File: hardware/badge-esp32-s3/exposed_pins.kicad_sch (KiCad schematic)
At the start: 0 parts

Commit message: JST PH and JST SH headers completed
Both subsheets are in exposed pins subsheet. I also had to make the symbols and footprints associated with each other.
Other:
- added sheet JST PH (JST-PH.kicad_sch)
- added sheet JST-SH (JST-SH.kicad_sch)
- note added: "Grove Link"
- note added: "Refrence Pics for both Grove, Stemma, Stemma QT"
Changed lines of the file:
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@@
 	(generator_version "9.0")
 	(paper "A4")
+	(text "Refrence Pics for both Grove, Stemma, Stemma QT\n "
+		(exclude_from_sim no)
+		(at 71.374 32.766 0)
+		(effects
+			(font
+				(size 1.27 1.27)
+			)
+			(href "https://www.cable-tester.com/category/pin-out/")
+		)
+	)
+	(text "Grove Link\n\n"
+		(exclude_from_sim no)
+		(at 57.912 27.94 0)
+		(effects
+			(font
+				(size 1.27 1.27)
+			)
+			(href "https://wiki.seeedstudio.com/Grove_System/")
+		)
+	)
+	(sheet
+		(at 80.01 40.64)
+		(size 20.32 10.16)
+		(exclude_from_sim no)
+		(in_bom yes)
+		(on_board yes)
+		(dnp no)
+		(fields_autoplaced yes)
+		(stroke
+			(width 0.1524)
+			(type solid)
+		)
+		(fill
+			(color 0 0 0 0.0000)
+		)
+		(property "Sheetname" "JST-SH"
+			(at 80.01 39.9284 0)
+			(effects
+				(font
+					(size 1.27 1.27)
+				)
+				(justify left bottom)
+			)
+		)
+		(property "Sheetfile" "JST-SH.kicad_sch"
+			(at 80.01 51.3846 0)
+			(effects
+				(font
+					(size 1.27 1.27)
+				)
+				(justify left top)
+			)
+		)
+		(instances
+			(project "badge-esp32-s3"
+				(path "/e2af9a6c-dbe9-4de2-9ba6-ea213a7300ec/069334c8-a377-4249-b519-18db4f2b1959"
+					(page "16")
+				)
+			)
+		)
+	)
+	(sheet
+		(at 44.45 40.64)
+		(size 21.59 10.16)
+		(exclude_from_sim no)
+		(in_bom yes)
+		(on_board yes)
+		(dnp no)
+		(fields_autoplaced yes)
+		(stroke
+			(width 0.1524)
+			(type solid)
+		)
+		(fill
+			(color 0 0 0 0.0000)
+		)
+		(property "Sheetname" "JST PH"
+			(at 44.45 39.9284 0)
+			(effects
+				(font
+					(size 1.27 1.27)
+				)
+				(justify left bottom)
+			)
+		)
+		(property "Sheetfile" "JST-PH.kicad_sch"
+			(at 44.45 51.3846 0)
+			(effects
+				(font
+					(size 1.27 1.27)
+				)
+				(justify left top)
+			)
+		)
+		(instances
+			(project "badge-esp32-s3"
+				(path "/e2af9a6c-dbe9-4de2-9ba6-ea213a7300ec/069334c8-a377-4249-b519-18db4f2b1959"
+					(page "15")
+				)
+			)
+		)
+	)
 )

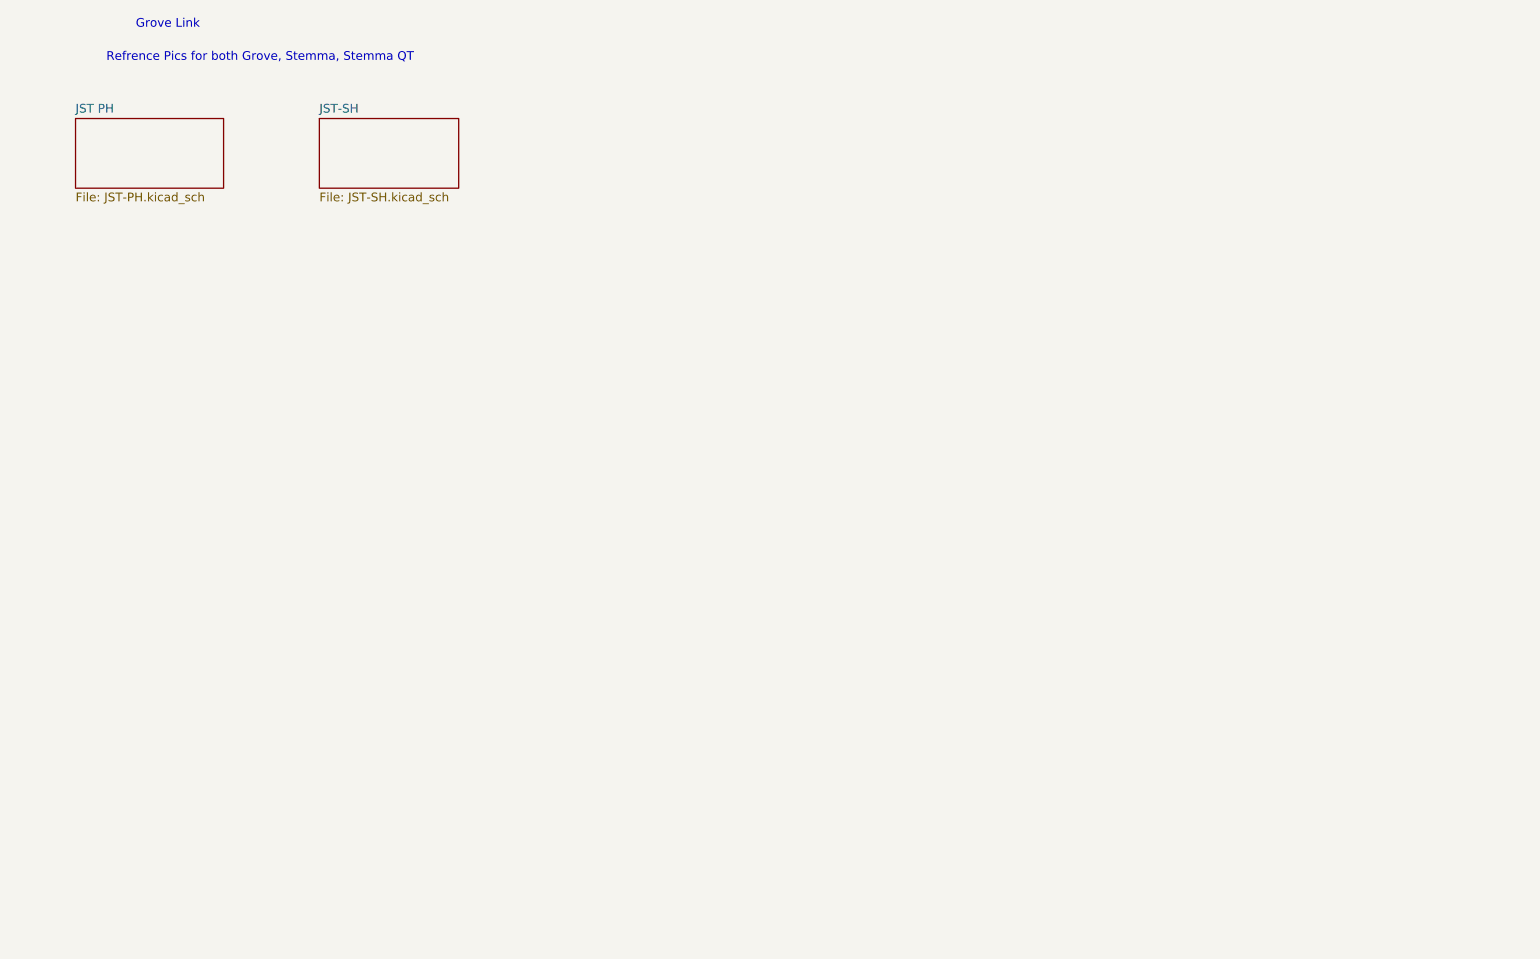
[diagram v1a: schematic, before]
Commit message: Fleshed out schematic with all exposed pins
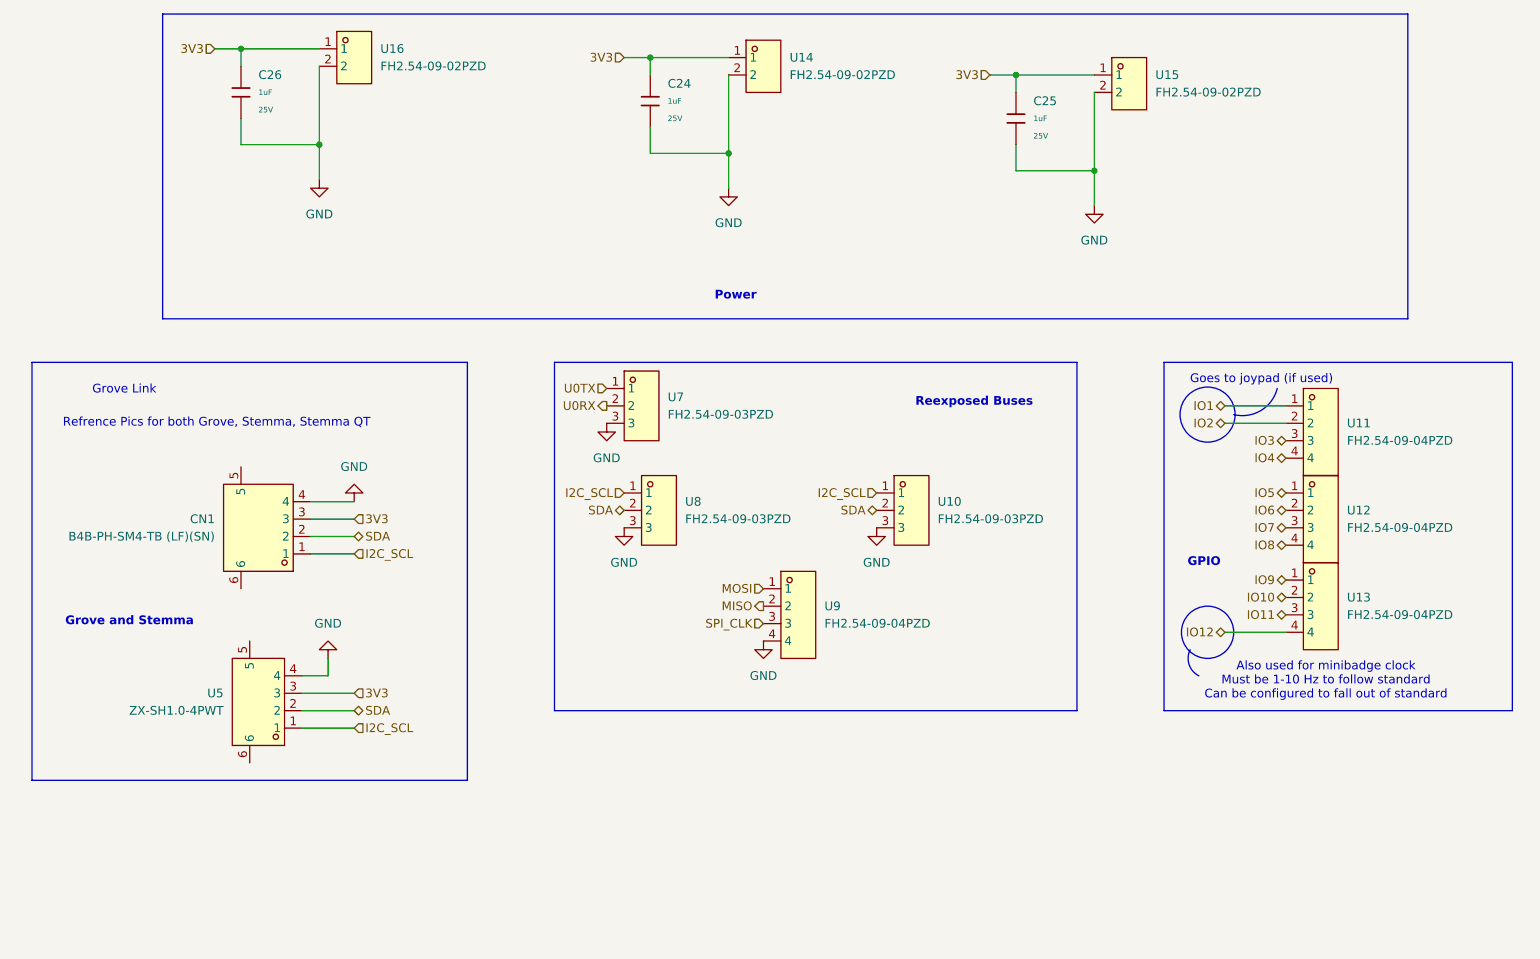
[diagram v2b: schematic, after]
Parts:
- added C24, C25, C26: 1uF, PCM_JLCPCB:C_0402, symbol PCM_JLCPCB-Capacitors:0402,1uF
- added CN1: B4B-PH-SM4-TB (LF)(SN), lcsc-lib:CONN-SMD_B4B-PH-SM4-TB-LF-SN, symbol lcsc-lib:B4B-PH-SM4-TB(LF)(SN)
- added U10, U7, U8: FH2.54-09-03PZD, lcsc-lib:HDR-TH_3P-P2.54-V-F, symbol lcsc-lib:FH2.54-09-03PZD
- added U11, U12, U13, U9: FH2.54-09-04PZD, lcsc-lib:HDR-TH_4P-P2.54-V-F, symbol lcsc-lib:FH2.54-09-04PZD
- added U14, U15, U16: FH2.54-09-02PZD, lcsc-lib:HDR-TH_2P-P2.54-V-M-5, symbol lcsc-lib:FH2.54-09-02PZD
- added U5: ZX-SH1.0-4PWT, lcsc-lib:CONN-SMD_4P-P1.00_MEGASTAR_ZX-SH1.0-4PWT, symbol lcsc-lib:ZX-SH1.0-4PWT
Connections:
- new net 3V3: C24.1, C25.1, C26.1, CN1.3, U14.1, U15.1, U16.1, U5.3
- new net GND: C24.2, C25.2, C26.2, CN1.4, U10.3, U14.2, U15.2, U16.2, U5.4, U7.3, U8.3, U9.4
- new net I2C_SCL: CN1.1, U10.1, U5.1, U8.1
- new net IO1: U11.1
- new net IO10: U13.2
- new net IO11: U13.3
- new net IO12: U13.4
- new net IO2: U11.2
- new net IO3: U11.3
- new net IO4: U11.4
- new net IO5: U12.1
- new net IO6: U12.2
- new net IO7: U12.3
- new net IO8: U12.4
- new net IO9: U13.1
- new net MISO: U9.2
- new net MOSI: U9.1
- new net SDA: CN1.2, U10.2, U5.2, U8.2
- new net SPI_CLK: U9.3
- new net U0RX: U7.2
- new net U0TX: U7.1
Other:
- removed sheet JST PH
- removed sheet JST-SH
- note added: "Also used for minibadge clock Must be 1-10 Hz to follow standard Can be configured to fall out of standard"
- note added: "GPIO"
- note added: "Goes to joypad (if used)"
- note added: "Grove and Stemma"
- note added: "Power"
- note added: "Reexposed Buses"

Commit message: Annotate schematic
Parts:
- renumbered C26 to C15, C24 to C16, C25 to C17, U14 to U10, U9 to U11, U10 to U12, U15 to U13, U11 to U14, U12 to U15, U13 to U16, U5 to U6, U16 to U7, U7 to U8, U8 to U9
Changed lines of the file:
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@@
 		(dnp no)
 		(fields_autoplaced yes)
-		(property "Reference" "#PWR052"
+		(property "Reference" "#PWR049"
 			(at 144.78 123.19 0)
 			(effects
@@
 			(project ""
 				(path "/e2af9a6c-dbe9-4de2-9ba6-ea213a7300ec/069334c8-a377-4249-b519-18db4f2b1959"
-					(reference "#PWR052")
+					(reference "#PWR049")
 					(unit 1)
 				)
@@
 		(dnp no)
 		(fields_autoplaced yes)
-		(property "Reference" "U13"
+		(property "Reference" "U16"
 			(at 229.87 110.4899 0)
 			(effects
@@
 			(project ""
 				(path "/e2af9a6c-dbe9-4de2-9ba6-ea213a7300ec/069334c8-a377-4249-b519-18db4f2b1959"
-					(reference "U13")
+					(reference "U16")
 					(unit 1)
 				)
@@
 		(dnp no)
 		(fields_autoplaced yes)
-		(property "Reference" "#PWR049"
+		(property "Reference" "#PWR044"
 			(at 81.28 113.03 0)
 			(effects
@@
 			(project "badge-esp32-s3"
 				(path "/e2af9a6c-dbe9-4de2-9ba6-ea213a7300ec/069334c8-a377-4249-b519-18db4f2b1959"
-					(reference "#PWR049")
+					(reference "#PWR044")
 					(unit 1)
 				)
@@
 		(dnp no)
 		(fields_autoplaced yes)
-		(property "Reference" "U15"
+		(property "Reference" "U13"
 			(at 201.93 34.2899 0)
 			(effects
@@
 			(project "badge-esp32-s3"
 				(path "/e2af9a6c-dbe9-4de2-9ba6-ea213a7300ec/069334c8-a377-4249-b519-18db4f2b1959"
-					(reference "U15")
+					(reference "U13")
 					(unit 1)
 				)
@@
 		(dnp no)
 		(fields_autoplaced yes)
-		(property "Reference" "U12"
+		(property "Reference" "U15"
 			(at 229.87 97.7899 0)
 			(effects
@@
 			(project ""
 				(path "/e2af9a6c-dbe9-4de2-9ba6-ea213a7300ec/069334c8-a377-4249-b519-18db4f2b1959"
-					(reference "U12")
+					(reference "U15")
 					(unit 1)
 				)
@@
 		(dnp no)
 		(fields_autoplaced yes)
-		(property "Reference" "U14"
+		(property "Reference" "U10"
 			(at 148.59 31.7499 0)
 			(effects
@@
 			(project ""
 				(path "/e2af9a6c-dbe9-4de2-9ba6-ea213a7300ec/069334c8-a377-4249-b519-18db4f2b1959"
-					(reference "U14")
+					(reference "U10")
 					(unit 1)
 				)
@@
 		(dnp no)
 		(fields_autoplaced yes)
-		(property "Reference" "U10"
+		(property "Reference" "U12"
 			(at 170.18 96.5199 0)
 			(effects
@@
 			(project "badge-esp32-s3"
 				(path "/e2af9a6c-dbe9-4de2-9ba6-ea213a7300ec/069334c8-a377-4249-b519-18db4f2b1959"
-					(reference "U10")
+					(reference "U12")
 					(unit 1)
 				)
@@
 		(dnp no)
 		(fields_autoplaced yes)
-		(property "Reference" "#PWR050"
+		(property "Reference" "#PWR046"
 			(at 121.92 91.44 0)
 			(effects
@@
 			(project ""
 				(path "/e2af9a6c-dbe9-4de2-9ba6-ea213a7300ec/069334c8-a377-4249-b519-18db4f2b1959"
-					(reference "#PWR050")
+					(reference "#PWR046")
 					(unit 1)
 				)
@@
 		(dnp no)
 		(fields_autoplaced yes)
-		(property "Reference" "#PWR054"
+		(property "Reference" "#PWR048"
 			(at 139.7 57.15 0)
 			(effects
@@
 			(project ""
 				(path "/e2af9a6c-dbe9-4de2-9ba6-ea213a7300ec/069334c8-a377-4249-b519-18db4f2b1959"
-					(reference "#PWR054")
+					(reference "#PWR048")
 					(unit 1)
 				)
@@
 		(dnp no)
 		(fields_autoplaced yes)
-		(property "Reference" "C26"
+		(property "Reference" "C15"
 			(at 71.12 34.2899 0)
 			(effects
@@
 			(project "badge-esp32-s3"
 				(path "/e2af9a6c-dbe9-4de2-9ba6-ea213a7300ec/069334c8-a377-4249-b519-18db4f2b1959"
-					(reference "C26")
+					(reference "C15")
 					(unit 1)
 				)
@@
 		(dnp no)
 		(fields_autoplaced yes)
-		(property "Reference" "#PWR053"
+		(property "Reference" "#PWR050"
 			(at 161.29 106.68 0)
 			(effects
@@
 			(project "badge-esp32-s3"
 				(path "/e2af9a6c-dbe9-4de2-9ba6-ea213a7300ec/069334c8-a377-4249-b519-18db4f2b1959"
-					(reference "#PWR053")
+					(reference "#PWR050")
 					(unit 1)
 				)
@@
 		(dnp no)
 		(fields_autoplaced yes)
-		(property "Reference" "U16"
+		(property "Reference" "U7"
 			(at 88.9 30.4799 0)
 			(effects
@@
 			(project "badge-esp32-s3"
 				(path "/e2af9a6c-dbe9-4de2-9ba6-ea213a7300ec/069334c8-a377-4249-b519-18db4f2b1959"
-					(reference "U16")
+					(reference "U7")
 					(unit 1)
 				)
@@
 		(dnp no)
 		(fields_autoplaced yes)
-		(property "Reference" "U5"
+		(property "Reference" "U6"
 			(at 66.04 124.4599 0)
 			(effects
@@
 			(project "badge-esp32-s3"
 				(path "/e2af9a6c-dbe9-4de2-9ba6-ea213a7300ec/069334c8-a377-4249-b519-18db4f2b1959"
-					(reference "U5")
+					(reference "U6")
 					(unit 1)
 				)
@@
 		(dnp no)
 		(fields_autoplaced yes)
-		(property "Reference" "#PWR056"
+		(property "Reference" "#PWR043"
 			(at 80.01 55.88 0)
 			(effects
@@
 			(project "badge-esp32-s3"
 				(path "/e2af9a6c-dbe9-4de2-9ba6-ea213a7300ec/069334c8-a377-4249-b519-18db4f2b1959"
-					(reference "#PWR056")
+					(reference "#PWR043")
 					(unit 1)
 				)
@@
 		(dnp no)
 		(fields_autoplaced yes)
-		(property "Reference" "C24"
+		(property "Reference" "C16"
 			(at 130.81 35.5599 0)
 			(effects
@@
 			(project "badge-esp32-s3"
 				(path "/e2af9a6c-dbe9-4de2-9ba6-ea213a7300ec/069334c8-a377-4249-b519-18db4f2b1959"
-					(reference "C24")
+					(reference "C16")
 					(unit 1)
 				)
@@
 		(dnp no)
 		(fields_autoplaced yes)
-		(property "Reference" "U11"
+		(property "Reference" "U14"
 			(at 229.87 85.0899 0)
 			(effects
@@
 			(project ""
 				(path "/e2af9a6c-dbe9-4de2-9ba6-ea213a7300ec/069334c8-a377-4249-b519-18db4f2b1959"
-					(reference "U11")
+					(reference "U14")
 					(unit 1)
 				)
@@
 		(dnp no)
 		(fields_autoplaced yes)
-		(property "Reference" "U9"
+		(property "Reference" "U11"
 			(at 153.67 111.7599 0)
 			(effects
@@
 			(project ""
 				(path "/e2af9a6c-dbe9-4de2-9ba6-ea213a7300ec/069334c8-a377-4249-b519-18db4f2b1959"
-					(reference "U9")
+					(reference "U11")
 					(unit 1)
 				)
@@
 		(dnp no)
 		(fields_autoplaced yes)
-		(property "Reference" "U7"
+		(property "Reference" "U8"
 			(at 130.81 81.2799 0)
 			(effects
@@
 			(project ""
 				(path "/e2af9a6c-dbe9-4de2-9ba6-ea213a7300ec/069334c8-a377-4249-b519-18db4f2b1959"
-					(reference "U7")
+					(reference "U8")
 					(unit 1)
 				)
@@
 		(dnp no)
 		(fields_autoplaced yes)
-		(property "Reference" "#PWR048"
+		(property "Reference" "#PWR045"
 			(at 85.09 90.17 0)
 			(effects
@@
 			(project "badge-esp32-s3"
 				(path "/e2af9a6c-dbe9-4de2-9ba6-ea213a7300ec/069334c8-a377-4249-b519-18db4f2b1959"
-					(reference "#PWR048")
+					(reference "#PWR045")
 					(unit 1)
 				)
@@
 		(dnp no)
 		(fields_autoplaced yes)
-		(property "Reference" "C25"
+		(property "Reference" "C17"
 			(at 184.15 38.0999 0)
 			(effects
@@
 			(project "badge-esp32-s3"
 				(path "/e2af9a6c-dbe9-4de2-9ba6-ea213a7300ec/069334c8-a377-4249-b519-18db4f2b1959"
-					(reference "C25")
+					(reference "C17")
 					(unit 1)
 				)
@@
 		(dnp no)
 		(fields_autoplaced yes)
-		(property "Reference" "#PWR055"
+		(property "Reference" "#PWR051"
 			(at 193.04 59.69 0)
 			(effects
@@
 			(project "badge-esp32-s3"
 				(path "/e2af9a6c-dbe9-4de2-9ba6-ea213a7300ec/069334c8-a377-4249-b519-18db4f2b1959"
-					(reference "#PWR055")
+					(reference "#PWR051")
 					(unit 1)
 				)
@@
 		(dnp no)
 		(fields_autoplaced yes)
-		(property "Reference" "#PWR051"
+		(property "Reference" "#PWR047"
 			(at 124.46 106.68 0)
 			(effects
@@
 			(project ""
 				(path "/e2af9a6c-dbe9-4de2-9ba6-ea213a7300ec/069334c8-a377-4249-b519-18db4f2b1959"
-					(reference "#PWR051")
+					(reference "#PWR047")
 					(unit 1)
 				)
@@
 		(dnp no)
 		(fields_autoplaced yes)
-		(property "Reference" "U8"
+		(property "Reference" "U9"
 			(at 133.35 96.5199 0)
 			(effects
@@
 			(project ""
 				(path "/e2af9a6c-dbe9-4de2-9ba6-ea213a7300ec/069334c8-a377-4249-b519-18db4f2b1959"
-					(reference "U8")
-					(unit 1)
-				)
+					(reference "U9")
+					(unit 1)
+				)

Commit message: Fix some DRC errors
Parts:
- added U19: FH2.54-09-02PZD, lcsc-lib:HDR-TH_2P-P2.54-V-M-5, symbol lcsc-lib:FH2.54-09-02PZD
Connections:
- new net IO45: U19.1
- new net IO46: U19.2
- no-connect marks 0 -> 4
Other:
- note added: "Strapping pins (not for ordinary use)"
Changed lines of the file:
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@@
+	)
+	(rectangle
+		(start 119.38 140.97)
+		(end 163.83 161.29)
+		(stroke
+			(width 0)
+			(type default)
+		)
+		(fill
+			(type none)
+		)
 	)
 	(rectangle
@@
 		(exclude_from_sim no)
 		(at 217.424 78.74 0)
+		(effects
+			(font
+				(size 1.27 1.27)
+			)
+		)
+	)
+	(text "Strapping pins (not for ordinary use)"
+		(exclude_from_sim no)
+		(at 141.986 144.526 0)
 		(effects
 			(font
@@
 		(color 0 0 0 0)
 	)
+	(no_connect
+		(at 69.85 116.84)
+	)
+	(no_connect
+		(at 68.58 91.44)
+	)
+	(no_connect
+		(at 69.85 134.62)
+	)
+	(no_connect
+		(at 68.58 109.22)
+	)
 	(wire
 		(pts
@@
 		)
 	)
+	(hierarchical_label "IO45"
+		(shape bidirectional)
+		(at 130.81 152.4 180)
+		(effects
+			(font
+				(size 1.27 1.27)
+			)
+			(justify right)
+		)
+	)
 	(hierarchical_label "IO11"
 		(shape bidirectional)
@@
 		(shape input)
 		(at 177.8 34.29 180)
+		(effects
+			(font
+				(size 1.27 1.27)
+			)
+			(justify right)
+		)
+	)
+	(hierarchical_label "IO46"
+		(shape bidirectional)
+		(at 130.81 154.94 180)
 		(effects
 			(font
@@
 					(unit 1)
 				)
+			)
+		)
+	)
+	(symbol
+		(lib_id "lcsc-lib:FH2.54-09-02PZD")
+		(at 135.89 153.67 0)
+		(unit 1)
+		(exclude_from_sim no)
+		(in_bom yes)
+		(on_board yes)
+		(dnp no)
+		(fields_autoplaced yes)
+		(property "Reference" "U19"
+			(at 139.7 152.3999 0)
+			(effects
+				(font
+					(size 1.27 1.27)
+				)
+				(justify left)
+			)
+		)
+		(property "Value" "FH2.54-09-02PZD"
+			(at 139.7 154.9399 0)
+			(effects
+				(font
+					(size 1.27 1.27)
+				)
+				(justify left)
+			)
+		)
+		(property "Footprint" "lcsc-lib:HDR-TH_2P-P2.54-V-M-5"
+			(at 135.89 162.56 0)
+			(effects
+				(font
+					(size 1.27 1.27)
+				)
+				(hide yes)
+			)
+		)
+		(property "Datasheet" ""
+			(at 135.89 153.67 0)
+			(effects
+				(font
+					(size 1.27 1.27)
+				)
+				(hide yes)
+			)
+		)
+		(property "Description" ""
+			(at 135.89 153.67 0)
+			(effects
+				(font
+					(size 1.27 1.27)
+				)
+				(hide yes)
+			)
+		)
+		(property "LCSC Part" "C7500771"
+			(at 135.89 165.1 0)
+			(effects
+				(font
+					(size 1.27 1.27)
+				)
+				(hide yes)
+			)
+		)
+		(pin "2"
+		)
+		(pin "1"
+		)
+		(instances
+			(project ""
+				(path "/e2af9a6c-dbe9-4de2-9ba6-ea213a7300ec/069334c8-a377-4249-b519-18db4f2b1959"
+					(reference "U19")
+					(unit 1)
+				)
